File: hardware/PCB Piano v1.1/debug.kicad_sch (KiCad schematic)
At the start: 2 parts, among them J2 1x5 Pin Header, J7 Conn_02x10_Odd_Even

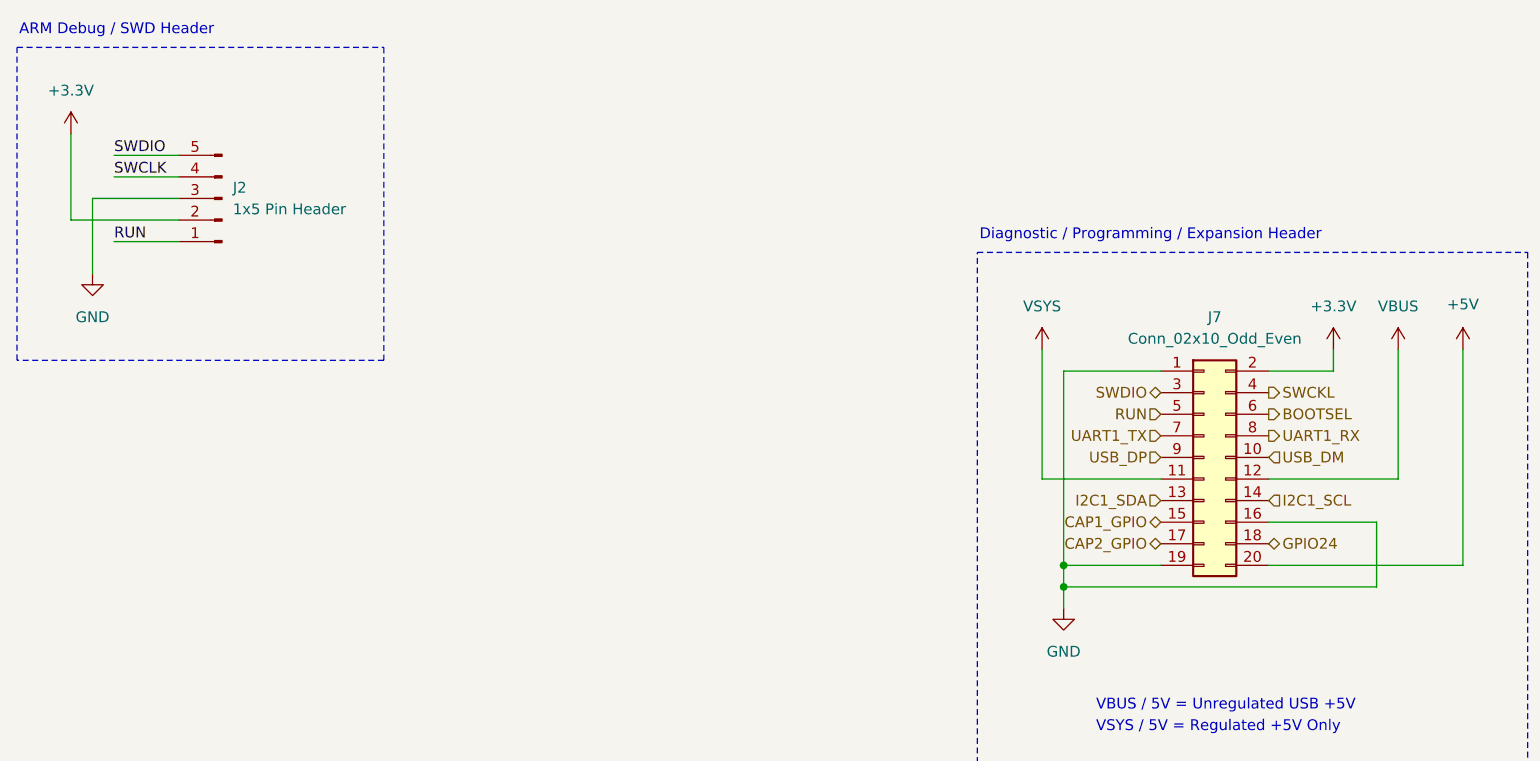
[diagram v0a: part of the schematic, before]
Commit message: Development Phase - PCB Complete - ERC/DRC in progress
Development commit. PBC layout complete. ERC/DRC checks in progress. Swapped some connectors for JST connectors with Adafruit-style polarization.
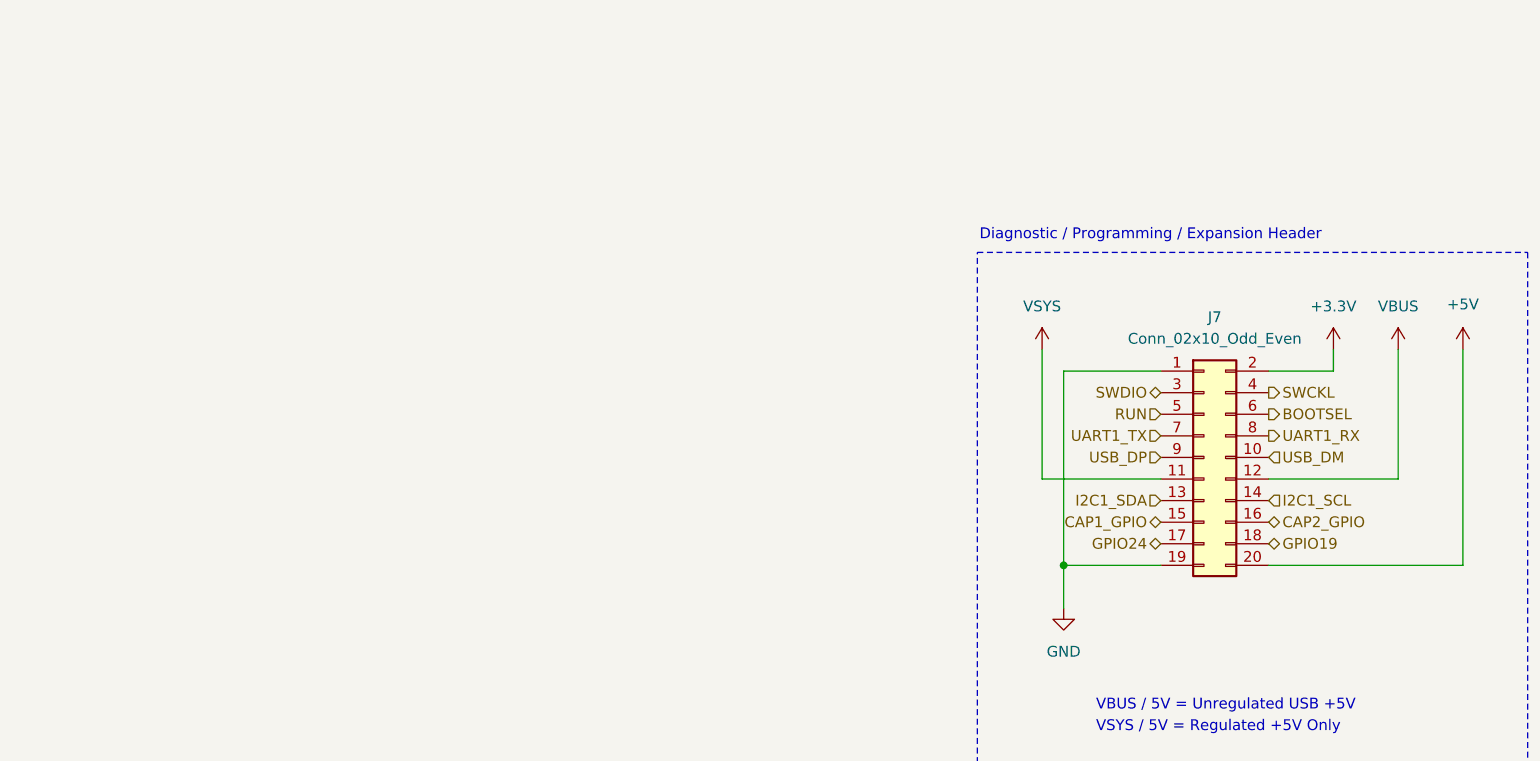
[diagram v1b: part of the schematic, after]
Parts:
- removed J2: 1x5 Pin Header, Connector_PinHeader_2.54mm:PinHeader_1x05_P2.54mm_Vertical_SMD_Pin1Left, symbol Connector:Conn_01x05_Pin
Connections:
- net CAP2_GPIO: now also J7.16 (Pin_16); no longer J7.17 (Pin_17)
- net GND: no longer J7.16 (Pin_16)
- net GPIO24: now also J7.17 (Pin_17); no longer J7.18 (Pin_18)
- new net GPIO19: J7.18 (Pin_18)
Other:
- note removed: "ARM Debug / SWD Header"

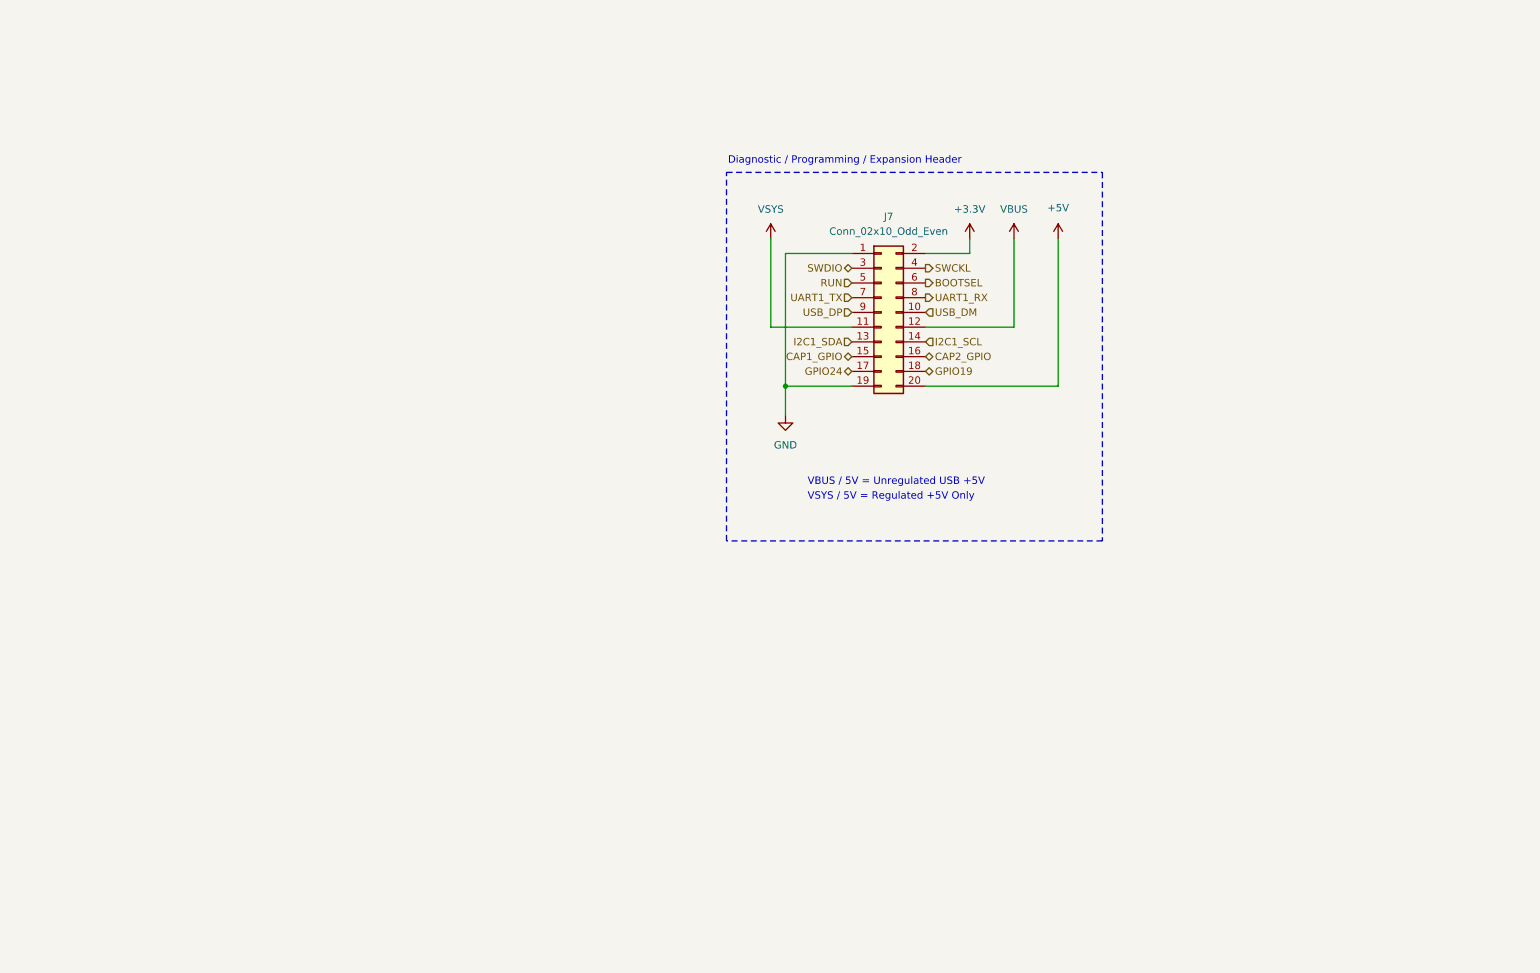
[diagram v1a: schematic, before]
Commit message: Firmware architecture complete - PCB revision with new charger.
Firmware Architecture Complete

- Added MP2724 charger driver
- Added TLV320DAC3100 driver
- Added MTCH2120 touch driver
- Added PCA9685 driver
- Added DotStar driver
- Added rotary encoder driver
- Added touch and LED maps
- Added control/audio/voice managers
- Added audio command queue
- Added Core1 audio architecture
- Added status LED system
- Added LED animation framework

Changes hardware schematic and PCB to accommodate a newer-style USB-C sink battery charger chip and USB data MUX to protect MCU while powered off.
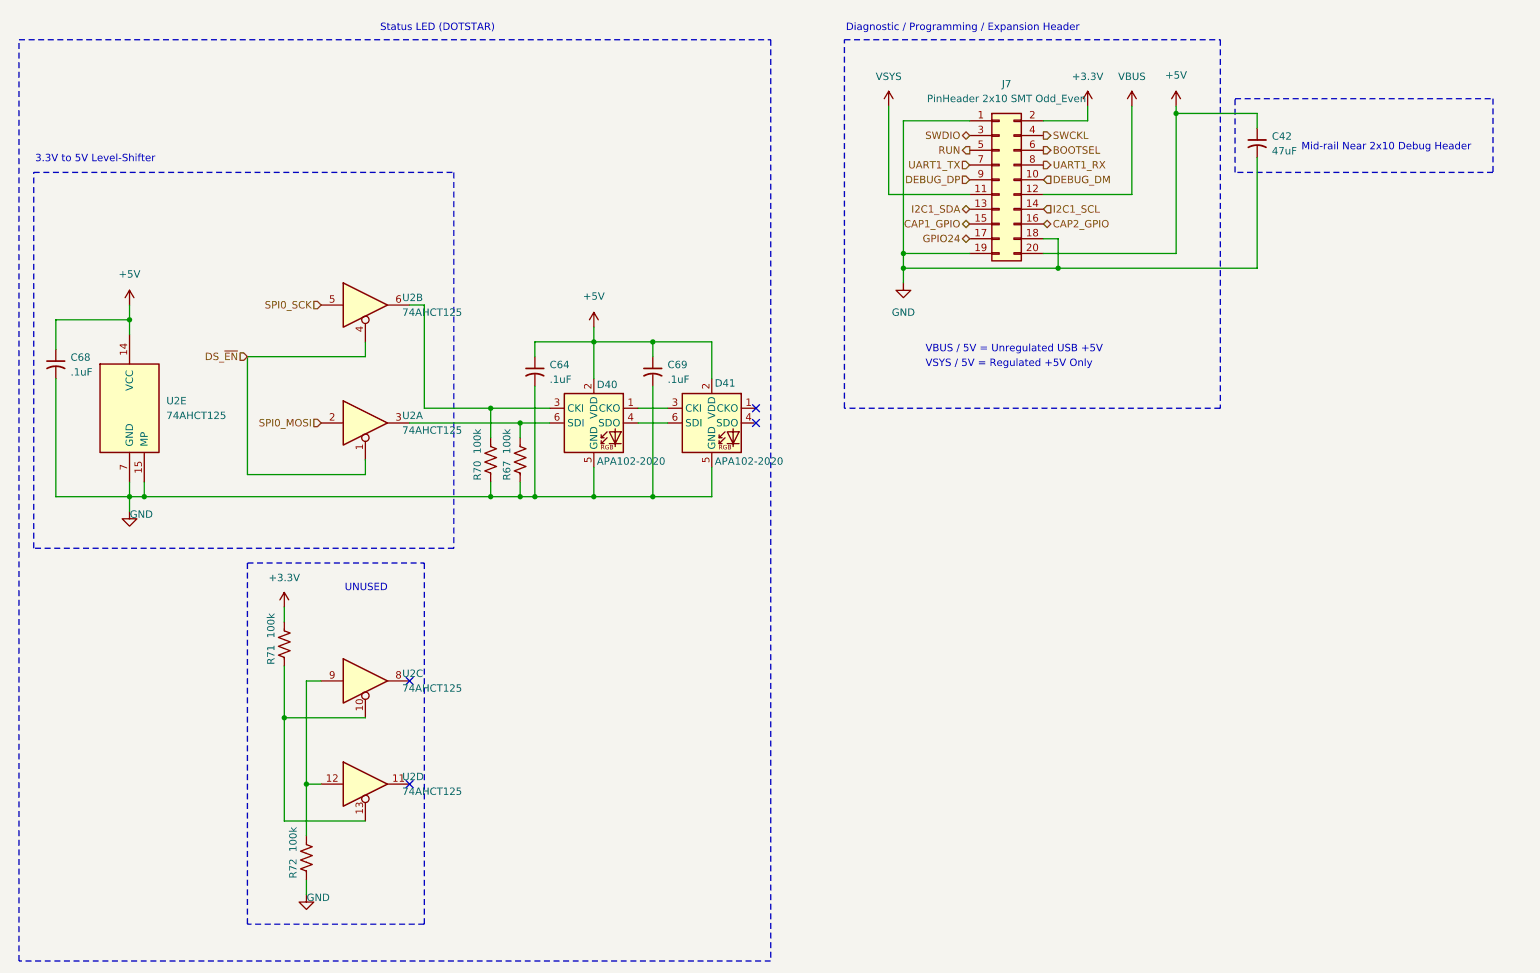
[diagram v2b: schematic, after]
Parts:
- added C42: 47uF, Capacitor_Tantalum_SMD:CP_EIA-3528-15_AVX-H, symbol Device:C_Small_US
- added C64, C68, C69: .1uF, Capacitor_SMD:C_0603_1608Metric, symbol Device:C_Small_US
- added D40, D41: APA102-2020, PCBPiano_Footprints:APA102-2020, symbol PCB_Piano_Symbols:APA102-2020
- added R67, R70, R71, R72: 100k, Resistor_SMD:R_0603_1608Metric, symbol Device:R_US
- added U2: 74AHCT125, Package_DFN_QFN:DHVQFN-14-1EP_2.5x3mm_P0.5mm_EP1x1.5mm, symbol 74xx:74AHCT125
- J7: value Conn_02x10_Odd_Even -> PinHeader 2x10 SMT Odd_Even
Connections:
- net GPIO19 is gone; now on net GND: J7.18 (Pin_18)
- net +3.3V: now also R71.1
- net +5V: now also C42.1, C64.1, C68.1, C69.1, D40.2 (VDD), D41.2 (VDD), U2.14 (VCC)
- net GND: now also C42.2, C64.2, C68.2, C69.2, D40.5 (GND), D41.5 (GND), R67.2, R70.2, R72.2, U2.15 (MP), U2.7 (GND)
- net USB_DM renamed DEBUG_DM
- net USB_DP renamed DEBUG_DP
- new net: D40.1 (CKO), D41.3 (CKI)
- new net: D40.3 (CKI), R70.1, U2.6
- new net: D40.4 (SDO), D41.6 (SDI)
- new net: D40.6 (SDI), R67.1, U2.3
- new net: R72.1, U2.12, U2.9
- new net: R71.2, U2.10, U2.13
- new net DS_~{EN}: U2.1, U2.4
- new net SPI0_MOSI: U2.2
- new net SPI0_SCK: U2.5
- no-connect marks 0 -> 4
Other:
- note added: "3.3V to 5V Level-Shifter"
- note added: "Mid-rail Near 2x10 Debug Header"
- note added: "Status LED (DOTSTAR)"
- note added: "UNUSED"
- moved on the sheet: J7

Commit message: PCB Finalized and Ordered. Firmware near completion.
PCB Finalized and Ordered. Final revisions included fixing bugs on some peripheral chips. Also added an RTC circuit after realizing the SD card could benefit from adding file timestamps.

Firmware near completion. Still need to finalize some SD card operations. Synth audio core is finished and all the board peripheral chip drivers were completed.
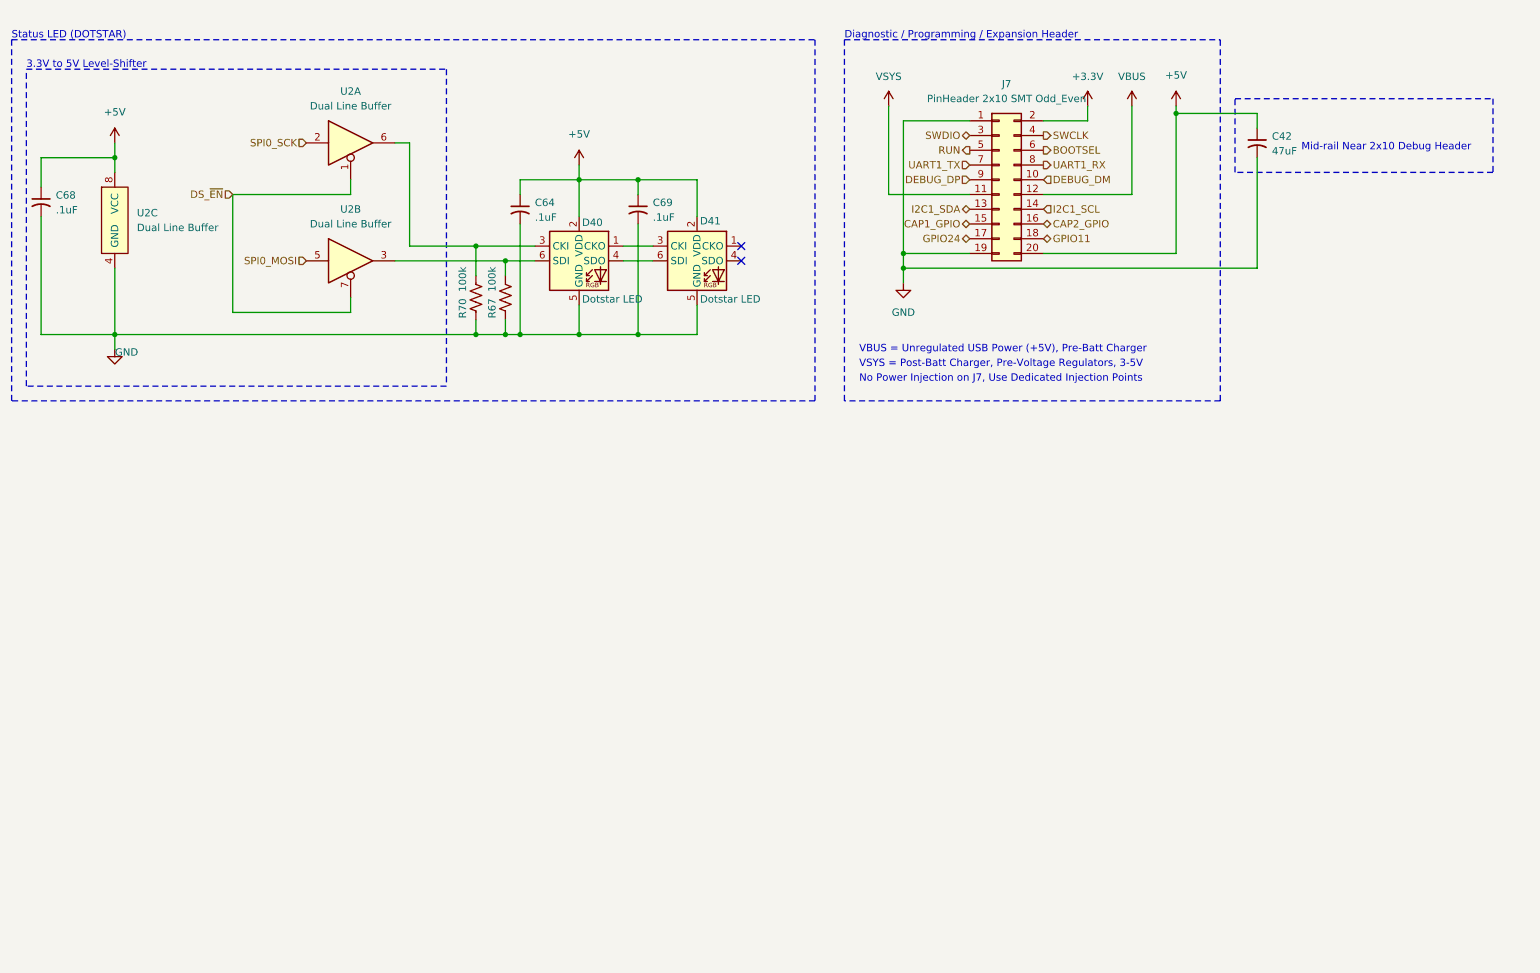
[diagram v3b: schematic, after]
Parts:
- removed R71, R72: 100k, Resistor_SMD:R_0603_1608Metric, symbol Device:R_US
- removed U2: 74AHCT125, Package_DFN_QFN:DHVQFN-14-1EP_2.5x3mm_P0.5mm_EP1x1.5mm, symbol 74xx:74AHCT125
- added U2: Dual Line Buffer, Package_SO:VSSOP-8_2.3x2mm_P0.5mm, symbol PCB Piano Symbols:74AHCT2G125
- C42: DigiKey_Part_Number (none) -> TAJB476K010RNJ; Manufacturer Part Number (none) -> TAJB476K010RNJ; Volt Rating (none) -> 10V
- C64, C68, C69: DigiKey_Part_Number (none) -> 1276-1935-2-ND; Manufacturer Part Number (none) -> CL10B104KB8NNWC; Volt Rating (none) -> 10V
- D40, D41: value APA102-2020 -> Dotstar LED; DigiKey_Part_Number (none) -> APA102-2020; Manufacturer Part Number (none) -> APA102-2020
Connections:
- net +5V: now also U2.8 (VCC)
- net DS_~{EN}: now also U2.1, U2.7
- net GND: now also U2.4 (GND); no longer J7.18 (Pin_18)
- net SPI0_MOSI: now also U2.5
- net SPI0_SCK: now also U2.2
- net at D40.3 (CKI), R70.1: now also U2.6
- net at D40.6 (SDI), R67.1: now also U2.3
- net SWCKL renamed SWCLK
- new net GPIO11: J7.18 (Pin_18)
- no-connect marks 4 -> 2
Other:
- note added: "No Power Injection on J7, Use Dedicated Injection Points"
- note added: "VBUS = Unregulated USB Power (+5V), Pre-Batt Charger"
- note added: "VSYS = Post-Batt Charger, Pre-Voltage Regulators, 3-5V"
- note removed: "UNUSED"
- note removed: "VBUS / 5V = Unregulated USB +5V"
- note removed: "VSYS / 5V = Regulated +5V Only"
- moved on the sheet: C64, C68, C69, D40, D41, R67, R70
